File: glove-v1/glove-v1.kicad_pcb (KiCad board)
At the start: 2 copper layers, 15 x 20 mm, 24 parts, among them J1 Conn_01x05, Q1 Q_PMOS_GSD, Q2 Q_Photo_NPN_EC, SW1 SW_Push, U1 LIS3DH, U2 STM32L031G6Ux

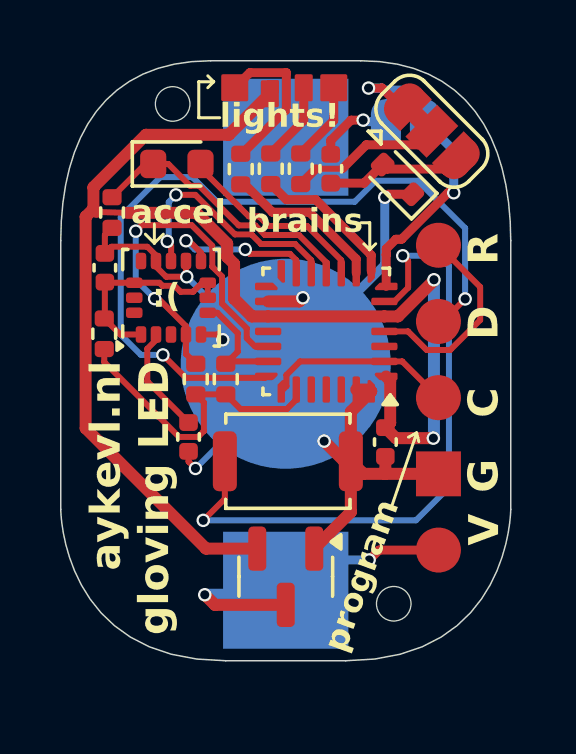
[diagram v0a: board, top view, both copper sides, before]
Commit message: fibonacci64: first version!
I produced this, and it works at least partially. The code is copied
from earring-ring-rgb36 which lights up around half the LEDs.

There's a few things that need changes though.
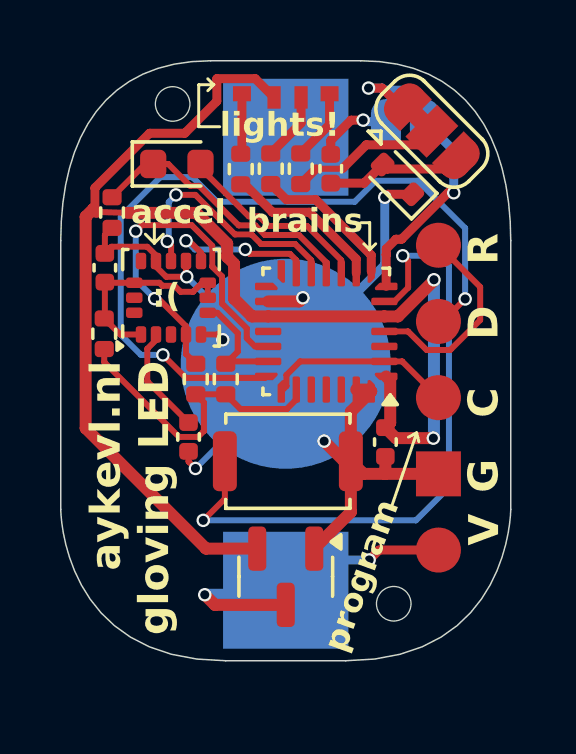
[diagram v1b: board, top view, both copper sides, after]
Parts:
- D1: value LED_BGAR -> LED_RAGB; footprint Custom:OSRAM_KRTB_AILMS1 -> Custom:FM-3510RGBA-SG
- moved D1 0.29 mm to (0.00, -4.84), turned to 0 degrees
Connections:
- D1 pad 1: Net-(D1-BK) -> Net-(D1-RK)
- D1 pad 2: Net-(D1-GK) -> VCC
- D1 pad 3: VCC -> Net-(D1-GK)
- D1 pad 4: Net-(D1-RK) -> Net-(D1-BK)
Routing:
- net Net-(D1-RK): track 5.29 -> 2.02 mm
- net VCC: track 44.8 -> 45.9 mm
